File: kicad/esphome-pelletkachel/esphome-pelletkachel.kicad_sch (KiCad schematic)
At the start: 18 parts, among them J1 Display-MCU-Connector, J2 Display-MCU-Connector, J3 MOSI-RSTSKIMIS, J4 Thumbs, U1 ESP32-DEVKITC-32U, U2 757, U3 VL53L0CXV0DH1

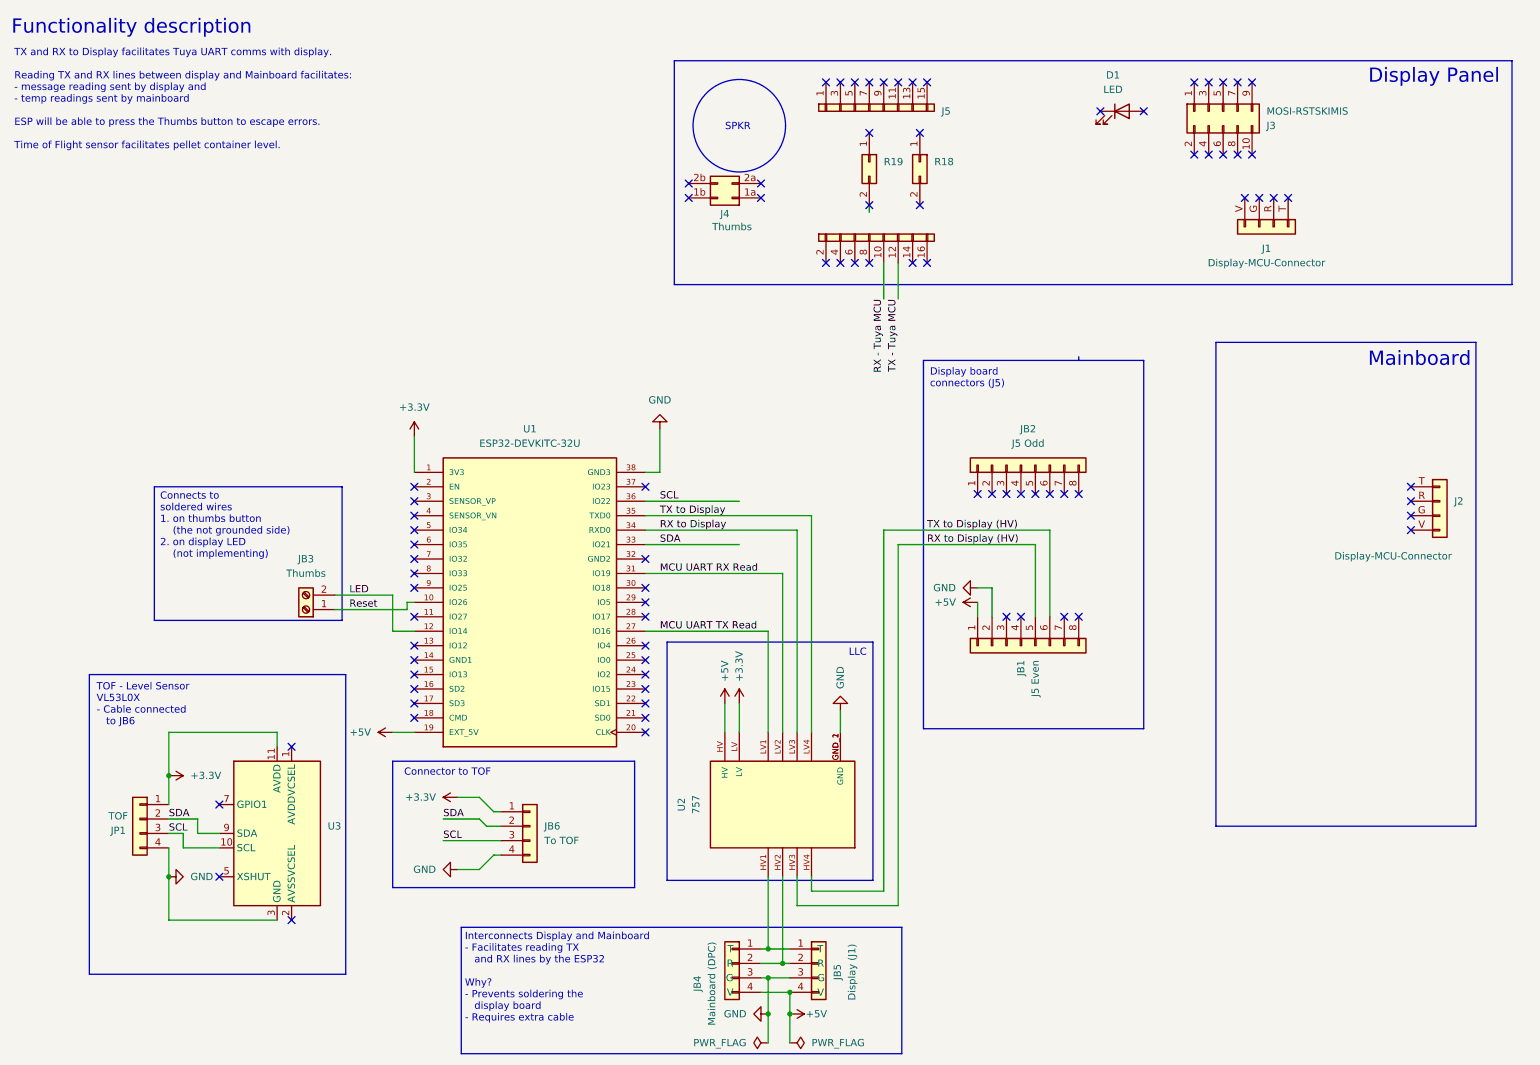
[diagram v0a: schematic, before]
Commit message: added tx rx switching method
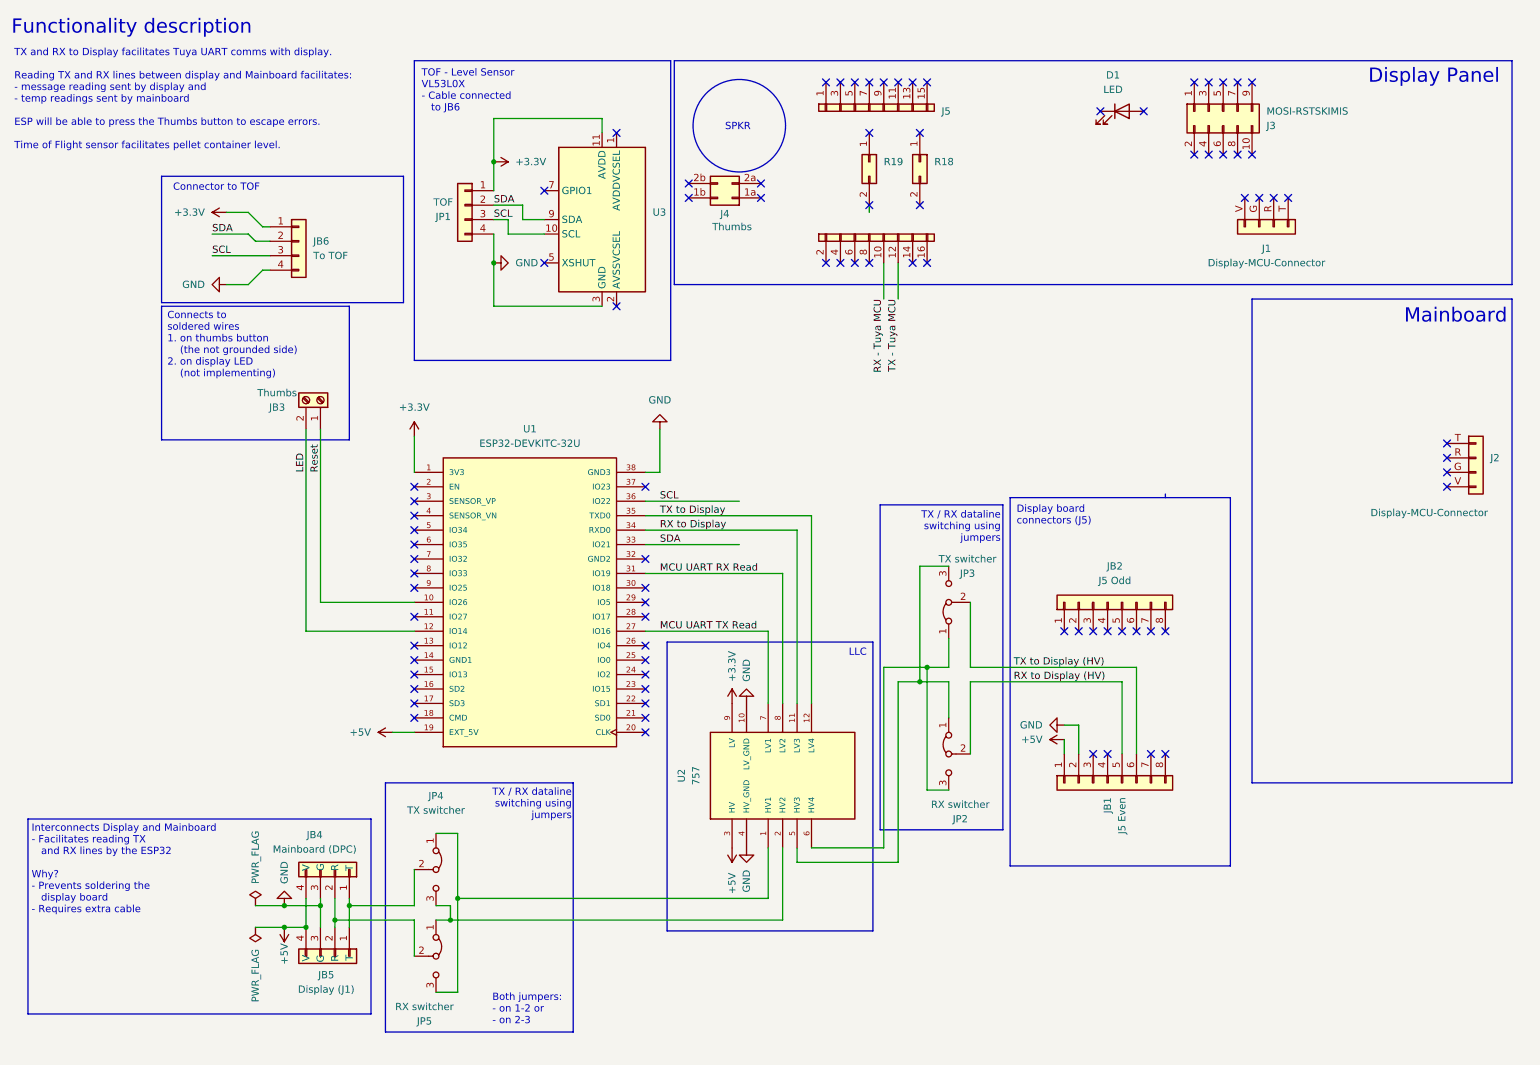
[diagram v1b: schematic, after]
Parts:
- added JP2, JP5: RX switcher, Connector_PinHeader_2.54mm:PinHeader_1x03_P2.54mm_Vertical, symbol Jumper:Jumper_3_Bridged12
- added JP3, JP4: TX switcher, Connector_PinHeader_2.54mm:PinHeader_1x03_P2.54mm_Vertical, symbol Jumper:Jumper_3_Bridged12
- U2: footprint 757:MODULE_757 -> Ron-Custom-Components:TT-4chLLC-SKU000275
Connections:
- net +3.3V: now also U2.9 (LV); no longer U2.LV
- net +5V: now also U2.3 (HV); no longer U2.HV
- net GND: now also U2.10 (LV_GND), U2.4 (HV_GND); no longer U2.GND_1 (GND), U2.GND_2 (GND)
- net MCU UART RX Read: now also U2.8 (LV2); no longer U2.LV2
- net MCU UART TX Read: now also U2.7 (LV1); no longer U2.LV1
- net RX to Display: now also U2.11 (LV3); no longer U2.LV3
- net RX to Display (HV): now also JP2.2 (C); no longer U2.HV3
- net TX to Display: now also U2.12 (LV4); no longer U2.LV4
- net TX to Display (HV): now also JP3.2 (C); no longer U2.HV4
- net at JB4.1 (T), JB5.1 (T): now also JP4.2 (C); no longer U2.HV1
- net at JB4.2 (R), JB5.2 (R): now also JP5.2 (C); no longer U2.HV2
- new net: JP2.1 (A), JP3.3 (B), U2.5 (HV3)
- new net: JP2.3 (B), JP3.1 (A), U2.6 (HV4)
- new net: JP4.1 (A), JP5.3 (B), U2.1 (HV1)
- new net: JP4.3 (B), JP5.1 (A), U2.2 (HV2)
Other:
- note added: "Both jumpers: - on 1-2 or - on 2-3"
- note added: "TX / RX dataline switching using jumpers"
- moved on the sheet: J2, JB1, JB2, JB3, JB4, JB5, JB6, JP1, U3

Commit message: zooo
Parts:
- removed JP4: TX switcher, Connector_PinHeader_2.54mm:PinHeader_1x03_P2.54mm_Vertical, symbol Jumper:Jumper_3_Bridged12
- removed JP5: RX switcher, Connector_PinHeader_2.54mm:PinHeader_1x03_P2.54mm_Vertical, symbol Jumper:Jumper_3_Bridged12
- added J6: 1-wire, Connector_PinHeader_2.54mm:PinHeader_1x03_P2.54mm_Vertical, symbol Connector_Generic:Conn_01x03
- added R1: 1k, Resistor_THT:R_Axial_DIN0204_L3.6mm_D1.6mm_P5.08mm_Horizontal, symbol Device:R
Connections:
- net +3.3V: now also J6.1 (Pin_1)
- net GND: now also J6.3 (Pin_3)
- net at U1.37 (IO23): now also R1.1
- net MCUTX: now reaches JB4.1 (T), JB5.1 (T)
- net MCUTX: now also U2.1 (HV1)
- net MCURX: now reaches JB4.2 (R), JB5.2 (R)
- net MCURX: now also U2.2 (HV2)
- new net: J6.2 (Pin_2), R1.2
- no-connect marks 85 -> 84
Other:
- note removed: "Both jumpers: - on 1-2 or - on 2-3"
- moved on the sheet: JB4, JB5

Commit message: changes
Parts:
- JP2, JP3: footprint Connector_PinHeader_2.54mm:PinHeader_1x03_P2.54mm_Vertical -> Jumper:SolderJumper-3_P1.3mm_Bridged12_RoundedPad1.0x1.5mm
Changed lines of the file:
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@@
 			)
 		)
-		(property "Footprint" "Connector_PinHeader_2.54mm:PinHeader_1x03_P2.54mm_Vertical"
+		(property "Footprint" "Jumper:SolderJumper-3_P1.3mm_Bridged12_RoundedPad1.0x1.5mm"
 			(at 180.34 143.51 0)
 			(effects
@@
 			)
 		)
-		(property "Footprint" "Connector_PinHeader_2.54mm:PinHeader_1x03_P2.54mm_Vertical"
+		(property "Footprint" "Jumper:SolderJumper-3_P1.3mm_Bridged12_RoundedPad1.0x1.5mm"
 			(at 180.34 116.84 0)
 			(effects

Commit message: changes
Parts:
- JB3: footprint TerminalBlock:TerminalBlock_bornier-2_P5.08mm -> TerminalBlock:TerminalBlock_Xinya_XY308-2.54-2P_1x02_P2.54mm_Horizontal
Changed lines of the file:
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@@
 			)
 		)
-		(property "Footprint" "TerminalBlock:TerminalBlock_bornier-2_P5.08mm"
+		(property "Footprint" "TerminalBlock:TerminalBlock_Xinya_XY308-2.54-2P_1x02_P2.54mm_Horizontal"
 			(at 69.85 81.28 0)
 			(effects
